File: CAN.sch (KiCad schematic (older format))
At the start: 6 parts, among them U9 TLE7250VSJ

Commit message: Changed the 5V-Regulator
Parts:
- C28, C29: symbol C_Small -> device:C_Small
- JP1: symbol Jumper_NC_Small -> device:Jumper_NC_Small
- R20, R21: symbol R -> device:R
- U9: symbol TLE7250VSJ -> transceiver:TLE7250VSJ
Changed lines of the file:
@@
-EESchema Schematic File Version 2
-LIBS:power
-LIBS:device
-LIBS:switches
-LIBS:transistors
-LIBS:conn
-LIBS:linear
-LIBS:regul
-LIBS:74xx
-LIBS:analog_switches
-LIBS:texas
-LIBS:interface
-LIBS:philips
-LIBS:cypress
-LIBS:siliconi
-LIBS:opto
-LIBS:contrib
-LIBS:stm32s
-LIBS:transceiver
-LIBS:switchingR
-LIBS:ledDriver
-LIBS:jacks
-LIBS:sensors
+EESchema Schematic File Version 4
 LIBS:Hardware-cache
-EELAYER 25 0
+EELAYER 26 0
 EELAYER END
 $Descr A4 11693 8268
@@
 $EndDescr
 $Comp
-L +5V #PWR079
+L power:+5V #PWR079
 U 1 1 5A8476B7
 P 2050 1350
@@
 $EndComp
 $Comp
-L +3.3V #PWR080
+L power:+3.3V #PWR080
 U 1 1 5A8476BD
 P 1350 1350
@@
 $EndComp
 $Comp
-L C_Small C29
+L device:C_Small C29
 U 1 1 5A8476C5
 P 1900 1500
@@
 $EndComp
 $Comp
-L C_Small C28
+L device:C_Small C28
 U 1 1 5A8476CC
 P 1500 1500
@@
 $EndComp
 $Comp
-L R R20
+L device:R R20
 U 1 1 5A8476D3
 P 950 2200
@@
 CAN-Transceiver
 $Comp
-L GND #PWR081
+L power:GND #PWR081
 U 1 1 5A8476DB
 P 1700 2700
@@
 $EndComp
 $Comp
-L GND #PWR082
+L power:GND #PWR082
 U 1 1 5A8476E1
 P 1700 1600
@@
 $EndComp
 $Comp
-L GND #PWR083
+L power:GND #PWR083
 U 1 1 5A8476E7
 P 650 2250
@@
 $EndComp
 $Comp
-L TLE7250VSJ U9
+L transceiver:TLE7250VSJ U9
 U 1 1 5A8476ED
 P 1700 2150
@@
 $EndComp
 $Comp
-L R R21
+L device:R R21
 U 1 1 5A8476F4
 P 2700 2550
@@
 $EndComp
 $Comp
-L Jumper_NC_Small JP1
+L device:Jumper_NC_Small JP1
 U 1 1 5A84773B
 P 2400 2550

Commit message: Minor Bugfixes
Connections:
- wire segments 18 -> 23
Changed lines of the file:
@@
 	1200 2500 1100 2500
 Wire Wire Line
-	2050 1350 2050 1800
+	2050 1350 2050 1500
 Wire Wire Line
-	1350 1350 1350 1800
+	1350 1350 1350 1500
 Wire Wire Line
 	2050 1500 2000 1500
@@
 	1700 1600 1700 1500
 Wire Wire Line
-	1600 1500 1800 1500
+	1600 1500 1700 1500
 Connection ~ 1700 1500
 Connection ~ 1350 1500
@@
 	2200 2200 2850 2200
 Wire Wire Line
-	2250 2500 2250 3050
+	2250 2500 2250 2550
 Wire Wire Line
-	2850 2200 2850 3050
+	2850 2200 2850 2550
 Wire Wire Line
 	2250 2500 2200 2500
@@
 Text HLabel 2850 3050 3    60   Input ~ 0
 CAN_H
+Wire Wire Line
+	1700 1500 1800 1500
+Wire Wire Line
+	1350 1500 1350 1800
+Wire Wire Line
+	2050 1500 2050 1800
+Wire Wire Line
+	2250 2550 2250 3050
+Wire Wire Line
+	2850 2550 2850 3050
 $EndSCHEMATC

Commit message: Updated to the new libraries
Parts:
- C28, C29: symbol device:C_Small -> Device:C_Small
- JP1: symbol device:Jumper_NC_Small -> Device:Jumper_NC_Small
- R18: renamed from R20; symbol device:R -> Device:R
- R19: renamed from R21; symbol device:R -> Device:R
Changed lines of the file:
@@
 $EndDescr
 $Comp
-L power:+5V #PWR079
+L power:+5V #PWR078
 U 1 1 5A8476B7
 P 2050 1350
-F 0 "#PWR079" H 2050 1200 50  0001 C CNN
+F 0 "#PWR078" H 2050 1200 50  0001 C CNN
 F 1 "+5V" H 2050 1490 50  0000 C CNN
 F 2 "" H 2050 1350 50  0001 C CNN
@@
 $EndComp
 $Comp
-L power:+3.3V #PWR080
+L power:+3.3V #PWR075
 U 1 1 5A8476BD
 P 1350 1350
-F 0 "#PWR080" H 1350 1200 50  0001 C CNN
+F 0 "#PWR075" H 1350 1200 50  0001 C CNN
 F 1 "+3.3V" H 1350 1490 50  0000 C CNN
 F 2 "" H 1350 1350 50  0001 C CNN
@@
 $EndComp
 $Comp
-L device:C_Small C29
+L Device:C_Small C29
 U 1 1 5A8476C5
 P 1900 1500
@@
 $EndComp
 $Comp
-L device:C_Small C28
+L Device:C_Small C28
 U 1 1 5A8476CC
 P 1500 1500
@@
 $EndComp
 $Comp
-L device:R R20
+L Device:R R18
 U 1 1 5A8476D3
 P 950 2200
-F 0 "R20" V 850 2250 50  0000 C CNN
+F 0 "R18" V 850 2250 50  0000 C CNN
 F 1 "10k" V 950 2200 50  0000 C CNN
 F 2 "Resistors_SMD:R_0603" V 880 2200 50  0001 C CNN
@@
 CAN-Transceiver
 $Comp
-L power:GND #PWR081
+L power:GND #PWR077
 U 1 1 5A8476DB
 P 1700 2700
-F 0 "#PWR081" H 1700 2450 50  0001 C CNN
+F 0 "#PWR077" H 1700 2450 50  0001 C CNN
 F 1 "GND" H 1700 2550 50  0000 C CNN
 F 2 "" H 1700 2700 50  0001 C CNN
@@
 $EndComp
 $Comp
-L power:GND #PWR082
+L power:GND #PWR076
 U 1 1 5A8476E1
 P 1700 1600
-F 0 "#PWR082" H 1700 1350 50  0001 C CNN
+F 0 "#PWR076" H 1700 1350 50  0001 C CNN
 F 1 "GND" H 1700 1450 50  0000 C CNN
 F 2 "" H 1700 1600 50  0001 C CNN
@@
 $EndComp
 $Comp
-L power:GND #PWR083
+L power:GND #PWR074
 U 1 1 5A8476E7
 P 650 2250
-F 0 "#PWR083" H 650 2000 50  0001 C CNN
+F 0 "#PWR074" H 650 2000 50  0001 C CNN
 F 1 "GND" H 650 2100 50  0000 C CNN
 F 2 "" H 650 2250 50  0001 C CNN
@@
 $EndComp
 $Comp
-L device:R R21
+L Device:R R19
 U 1 1 5A8476F4
 P 2700 2550
-F 0 "R21" V 2780 2550 50  0000 C CNN
+F 0 "R19" V 2780 2550 50  0000 C CNN
 F 1 "120" V 2700 2550 50  0000 C CNN
 F 2 "Resistors_SMD:R_0603" V 2630 2550 50  0001 C CNN
@@
 $EndComp
 $Comp
-L device:Jumper_NC_Small JP1
+L Device:Jumper_NC_Small JP1
 U 1 1 5A84773B
 P 2400 2550

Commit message: Added Component-Associations (about 10% remaining)
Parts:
- C28, C29: Buy (none) -> https://www.digikey.com/product-detail/en/kemet/C0603C104M5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
- R18: Buy (none) -> https://www.digikey.com/product-detail/en/yageo/RC0603FR-07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
- R19: footprint Resistors_SMD:R_0603 -> Resistors_SMD:R_1206; Buy (none) -> https://www.digikey.com/product-detail/en/yageo/RC1206FR-07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
- U9: Buy (none) -> https://www.digikey.com/product-detail/en/infineon-technolo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
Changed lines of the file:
@@
 F 2 "Capacitors_SMD:C_0603" H 1900 1500 50  0001 C CNN
 F 3 "" H 1900 1500 50  0001 C CNN
+F 4 "https://www.digikey.com/product-detail/en/kemet/C0603C104M5RACTU/399-7845-1-ND/3471568" V 1900 1500 50  0001 C CNN "Buy"
 	1    1900 1500
 	0    1    1    0
@@
 F 2 "Capacitors_SMD:C_0603" H 1500 1500 50  0001 C CNN
 F 3 "" H 1500 1500 50  0001 C CNN
+F 4 "https://www.digikey.com/product-detail/en/kemet/C0603C104M5RACTU/399-7845-1-ND/3471568" V 1500 1500 50  0001 C CNN "Buy"
 	1    1500 1500
 	0    1    1    0
@@
 F 2 "Resistors_SMD:R_0603" V 880 2200 50  0001 C CNN
 F 3 "" H 950 2200 50  0001 C CNN
+F 4 "https://www.digikey.com/product-detail/en/yageo/RC0603FR-0710KL/311-10.0KHRCT-ND/729827" V 950 2200 50  0001 C CNN "Buy"
 	1    950  2200
 	0    1    1    0
@@
 F 2 "Housings_SOIC:SOIC-8_3.9x4.9mm_Pitch1.27mm" H 1700 1900 60  0001 C CNN
 F 3 "" H 1700 1900 60  0001 C CNN
+F 4 "https://www.digikey.com/product-detail/en/infineon-technologies/TLE7250VSJXUMA1/TLE7250VSJXUMA1CT-ND/6560083" H 1700 2150 50  0001 C CNN "Buy"
 	1    1700 2150
 	1    0    0    -1
@@
 F 0 "R19" V 2780 2550 50  0000 C CNN
 F 1 "120" V 2700 2550 50  0000 C CNN
-F 2 "Resistors_SMD:R_0603" V 2630 2550 50  0001 C CNN
+F 2 "Resistors_SMD:R_1206" V 2630 2550 50  0001 C CNN
 F 3 "" H 2700 2550 50  0001 C CNN
+F 4 "https://www.digikey.com/product-detail/en/yageo/RC1206FR-07120RL/311-120FRCT-ND/731470" V 2700 2550 50  0001 C CNN "Buy"
 	1    2700 2550
 	0    1    1    0

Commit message: Minor changes to layout and component association
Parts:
- C28, C29: Buy https://www.digikey.com/product-detail/en/kemet/C0603C104M5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 -> https://www.digikey.com/product-detail/en/kemet/C0603C104K3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
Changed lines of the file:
@@
 F 2 "Capacitors_SMD:C_0603" H 1900 1500 50  0001 C CNN
 F 3 "" H 1900 1500 50  0001 C CNN
-F 4 "https://www.digikey.com/product-detail/en/kemet/C0603C104M5RACTU/399-7845-1-ND/3471568" V 1900 1500 50  0001 C CNN "Buy"
+F 4 "https://www.digikey.com/product-detail/en/kemet/C0603C104K3RACTU/399-1281-1-ND/416057" V 1900 1500 50  0001 C CNN "Buy"
 	1    1900 1500
 	0    1    1    0
@@
 F 2 "Capacitors_SMD:C_0603" H 1500 1500 50  0001 C CNN
 F 3 "" H 1500 1500 50  0001 C CNN
-F 4 "https://www.digikey.com/product-detail/en/kemet/C0603C104M5RACTU/399-7845-1-ND/3471568" V 1500 1500 50  0001 C CNN "Buy"
+F 4 "https://www.digikey.com/product-detail/en/kemet/C0603C104K3RACTU/399-1281-1-ND/416057" V 1500 1500 50  0001 C CNN "Buy"
 	1    1500 1500
 	0    1    1    0

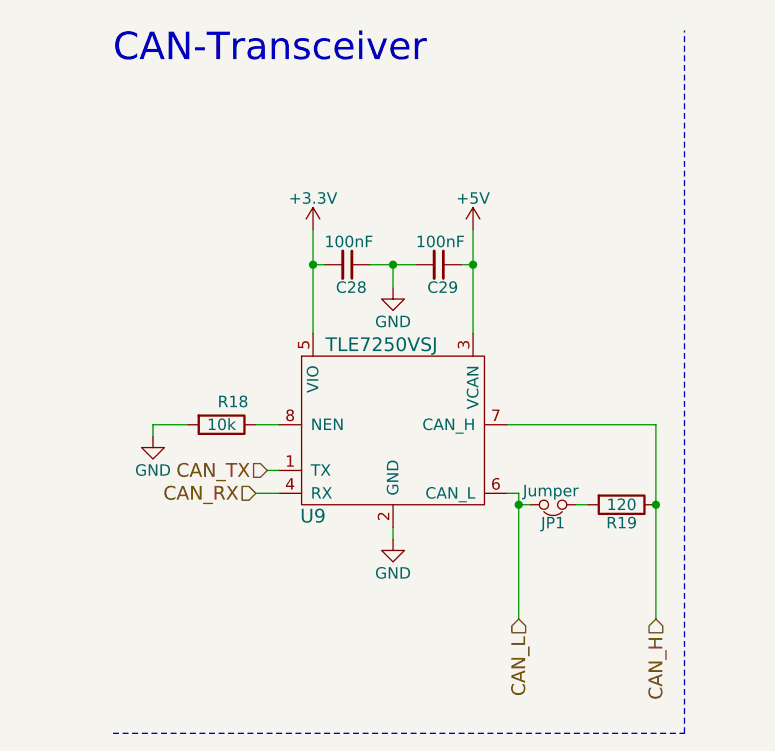
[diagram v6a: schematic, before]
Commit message: Added about 8% of the remaining components
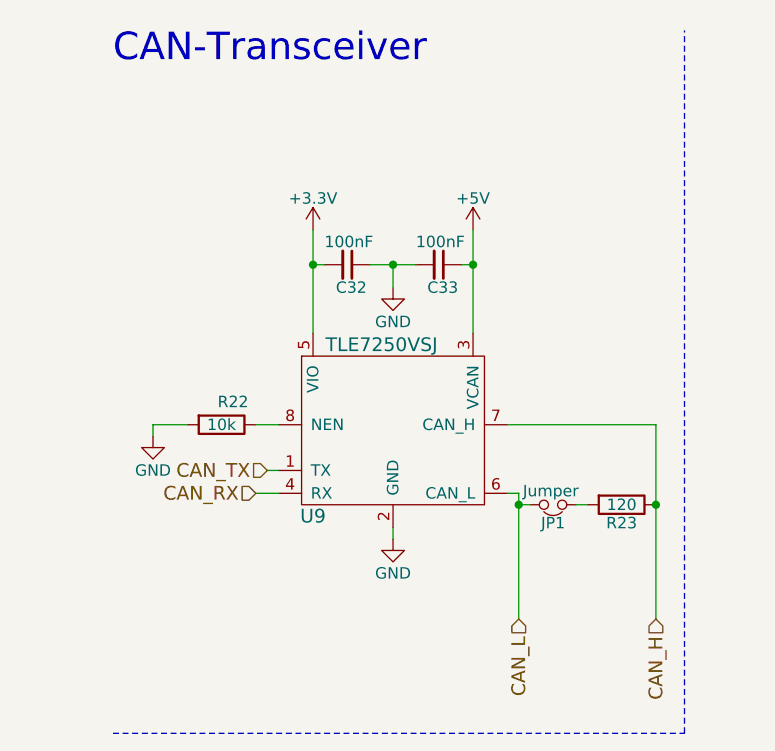
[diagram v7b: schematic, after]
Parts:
- renumbered C28 to C32, C29 to C33, R18 to R22, R19 to R23
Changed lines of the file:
@@
 $EndDescr
 $Comp
-L power:+5V #PWR081
+L power:+5V #PWR084
 U 1 1 5A8476B7
 P 2050 1350
-F 0 "#PWR081" H 2050 1200 50  0001 C CNN
+F 0 "#PWR084" H 2050 1200 50  0001 C CNN
 F 1 "+5V" H 2050 1490 50  0000 C CNN
 F 2 "" H 2050 1350 50  0001 C CNN
@@
 $EndComp
 $Comp
-L power:+3.3V #PWR078
+L power:+3.3V #PWR081
 U 1 1 5A8476BD
 P 1350 1350
-F 0 "#PWR078" H 1350 1200 50  0001 C CNN
+F 0 "#PWR081" H 1350 1200 50  0001 C CNN
 F 1 "+3.3V" H 1350 1490 50  0000 C CNN
 F 2 "" H 1350 1350 50  0001 C CNN
@@
 $EndComp
 $Comp
-L Device:C_Small C29
+L Device:C_Small C33
 U 1 1 5A8476C5
 P 1900 1500
-F 0 "C29" V 2000 1450 50  0000 L CNN
+F 0 "C33" V 2000 1450 50  0000 L CNN
 F 1 "100nF" V 1800 1400 50  0000 L CNN
 F 2 "Capacitors_SMD:C_0603" H 1900 1500 50  0001 C CNN
@@
 $EndComp
 $Comp
-L Device:C_Small C28
+L Device:C_Small C32
 U 1 1 5A8476CC
 P 1500 1500
-F 0 "C28" V 1600 1450 50  0000 L CNN
+F 0 "C32" V 1600 1450 50  0000 L CNN
 F 1 "100nF" V 1400 1400 50  0000 L CNN
 F 2 "Capacitors_SMD:C_0603" H 1500 1500 50  0001 C CNN
@@
 $EndComp
 $Comp
-L Device:R R18
+L Device:R R22
 U 1 1 5A8476D3
 P 950 2200
-F 0 "R18" V 850 2250 50  0000 C CNN
+F 0 "R22" V 850 2250 50  0000 C CNN
 F 1 "10k" V 950 2200 50  0000 C CNN
 F 2 "Resistors_SMD:R_0603" V 880 2200 50  0001 C CNN
@@
 CAN-Transceiver
 $Comp
-L power:GND #PWR080
+L power:GND #PWR083
 U 1 1 5A8476DB
 P 1700 2700
-F 0 "#PWR080" H 1700 2450 50  0001 C CNN
+F 0 "#PWR083" H 1700 2450 50  0001 C CNN
 F 1 "GND" H 1700 2550 50  0000 C CNN
 F 2 "" H 1700 2700 50  0001 C CNN
@@
 $EndComp
 $Comp
-L power:GND #PWR079
+L power:GND #PWR082
 U 1 1 5A8476E1
 P 1700 1600
-F 0 "#PWR079" H 1700 1350 50  0001 C CNN
+F 0 "#PWR082" H 1700 1350 50  0001 C CNN
 F 1 "GND" H 1700 1450 50  0000 C CNN
 F 2 "" H 1700 1600 50  0001 C CNN
@@
 $EndComp
 $Comp
-L power:GND #PWR077
+L power:GND #PWR080
 U 1 1 5A8476E7
 P 650 2250
-F 0 "#PWR077" H 650 2000 50  0001 C CNN
+F 0 "#PWR080" H 650 2000 50  0001 C CNN
 F 1 "GND" H 650 2100 50  0000 C CNN
 F 2 "" H 650 2250 50  0001 C CNN
@@
 $EndComp
 $Comp
-L Device:R R19
+L Device:R R23
 U 1 1 5A8476F4
 P 2700 2550
-F 0 "R19" V 2780 2550 50  0000 C CNN
+F 0 "R23" V 2780 2550 50  0000 C CNN
 F 1 "120" V 2700 2550 50  0000 C CNN
 F 2 "Resistors_SMD:R_1206" V 2630 2550 50  0001 C CNN

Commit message: Switch to new kicad footprint library
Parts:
- C32, C33: footprint Capacitors_SMD:C_0603 -> Capacitor_SMD:C_0603_1608Metric
- JP1: footprint Socket_Strips:Socket_Strip_Straight_2x01_Pitch2.54mm -> Connector_PinHeader_2.54mm:PinHeader_2x01_P2.54mm_Vertical
- R22: footprint Resistors_SMD:R_0603 -> Resistor_SMD:R_0603_1608Metric
- R23: footprint Resistors_SMD:R_1206 -> Resistor_SMD:R_1206_3216Metric
- U9: footprint Housings_SOIC:SOIC-8_3.9x4.9mm_Pitch1.27mm -> Package_SO:SOIC-8_3.9x4.9mm_P1.27mm
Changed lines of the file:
@@
 F 0 "C33" V 2000 1450 50  0000 L CNN
 F 1 "100nF" V 1800 1400 50  0000 L CNN
-F 2 "Capacitors_SMD:C_0603" H 1900 1500 50  0001 C CNN
+F 2 "Capacitor_SMD:C_0603_1608Metric" H 1900 1500 50  0001 C CNN
 F 3 "" H 1900 1500 50  0001 C CNN
 F 4 "https://www.digikey.com/product-detail/en/kemet/C0603C104K3RACTU/399-1281-1-ND/416057" V 1900 1500 50  0001 C CNN "Buy"
@@
 F 0 "C32" V 1600 1450 50  0000 L CNN
 F 1 "100nF" V 1400 1400 50  0000 L CNN
-F 2 "Capacitors_SMD:C_0603" H 1500 1500 50  0001 C CNN
+F 2 "Capacitor_SMD:C_0603_1608Metric" H 1500 1500 50  0001 C CNN
 F 3 "" H 1500 1500 50  0001 C CNN
 F 4 "https://www.digikey.com/product-detail/en/kemet/C0603C104K3RACTU/399-1281-1-ND/416057" V 1500 1500 50  0001 C CNN "Buy"
@@
 F 0 "R22" V 850 2250 50  0000 C CNN
 F 1 "10k" V 950 2200 50  0000 C CNN
-F 2 "Resistors_SMD:R_0603" V 880 2200 50  0001 C CNN
+F 2 "Resistor_SMD:R_0603_1608Metric" V 880 2200 50  0001 C CNN
 F 3 "" H 950 2200 50  0001 C CNN
 F 4 "https://www.digikey.com/product-detail/en/yageo/RC0603FR-0710KL/311-10.0KHRCT-ND/729827" V 950 2200 50  0001 C CNN "Buy"
@@
 F 0 "U9" H 1350 1700 60  0000 C CNN
 F 1 "TLE7250VSJ" H 1650 2450 60  0000 C CNN
-F 2 "Housings_SOIC:SOIC-8_3.9x4.9mm_Pitch1.27mm" H 1700 1900 60  0001 C CNN
+F 2 "Package_SO:SOIC-8_3.9x4.9mm_P1.27mm" H 1700 1900 60  0001 C CNN
 F 3 "" H 1700 1900 60  0001 C CNN
 F 4 "https://www.digikey.com/product-detail/en/infineon-technologies/TLE7250VSJXUMA1/TLE7250VSJXUMA1CT-ND/6560083" H 1700 2150 50  0001 C CNN "Buy"
@@
 F 0 "R23" V 2780 2550 50  0000 C CNN
 F 1 "120" V 2700 2550 50  0000 C CNN
-F 2 "Resistors_SMD:R_1206" V 2630 2550 50  0001 C CNN
+F 2 "Resistor_SMD:R_1206_3216Metric" V 2630 2550 50  0001 C CNN
 F 3 "" H 2700 2550 50  0001 C CNN
 F 4 "https://www.digikey.com/product-detail/en/yageo/RC1206FR-07120RL/311-120FRCT-ND/731470" V 2700 2550 50  0001 C CNN "Buy"
@@
 F 0 "JP1" H 2400 2630 50  0000 C CNN
 F 1 "Jumper" H 2410 2490 50  0000 C CNN
-F 2 "Socket_Strips:Socket_Strip_Straight_2x01_Pitch2.54mm" H 2400 2550 50  0001 C CNN
+F 2 "Connector_PinHeader_2.54mm:PinHeader_2x01_P2.54mm_Vertical" H 2400 2550 50  0001 C CNN
 F 3 "" H 2400 2550 50  0001 C CNN
 	1    2400 2550
